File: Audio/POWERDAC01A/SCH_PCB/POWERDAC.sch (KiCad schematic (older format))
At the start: 69 parts, among them J1 CONFIG, J10 BICKI, J11 SA, J12 +VS, J13 -VS, J14 RESET, J15 OUT3, J16 OUT4, J17 OUT1A, J18 OUT1B, J19 OUT2B, J2 DIGITAL POWER, J20 OUT2A, J3 PWRDN, J4 INT_LINE, J5 SDA, J6 SCL, J7 SDI, J8 LRCKI, J9 XTI, M1 HOLE, M2 HOLE, M3 HOLE, M4 HOLE, U1 STA350BW

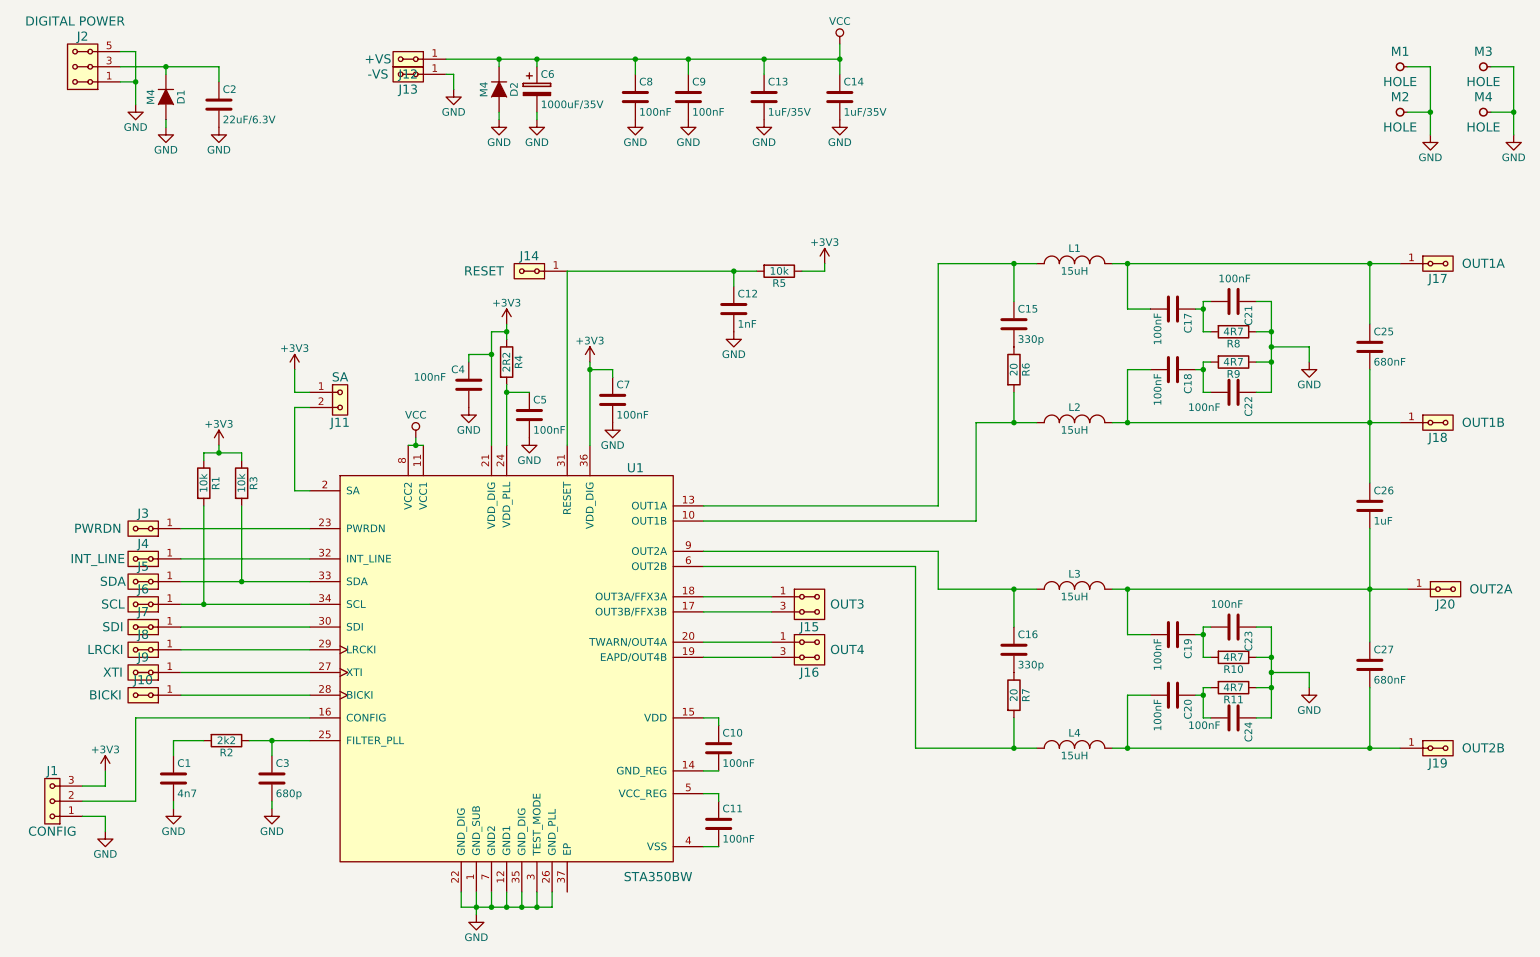
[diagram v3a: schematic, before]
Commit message: routovani plosneho spoje, Zmena zapojeni napajeni konfiguracnich vystupu.
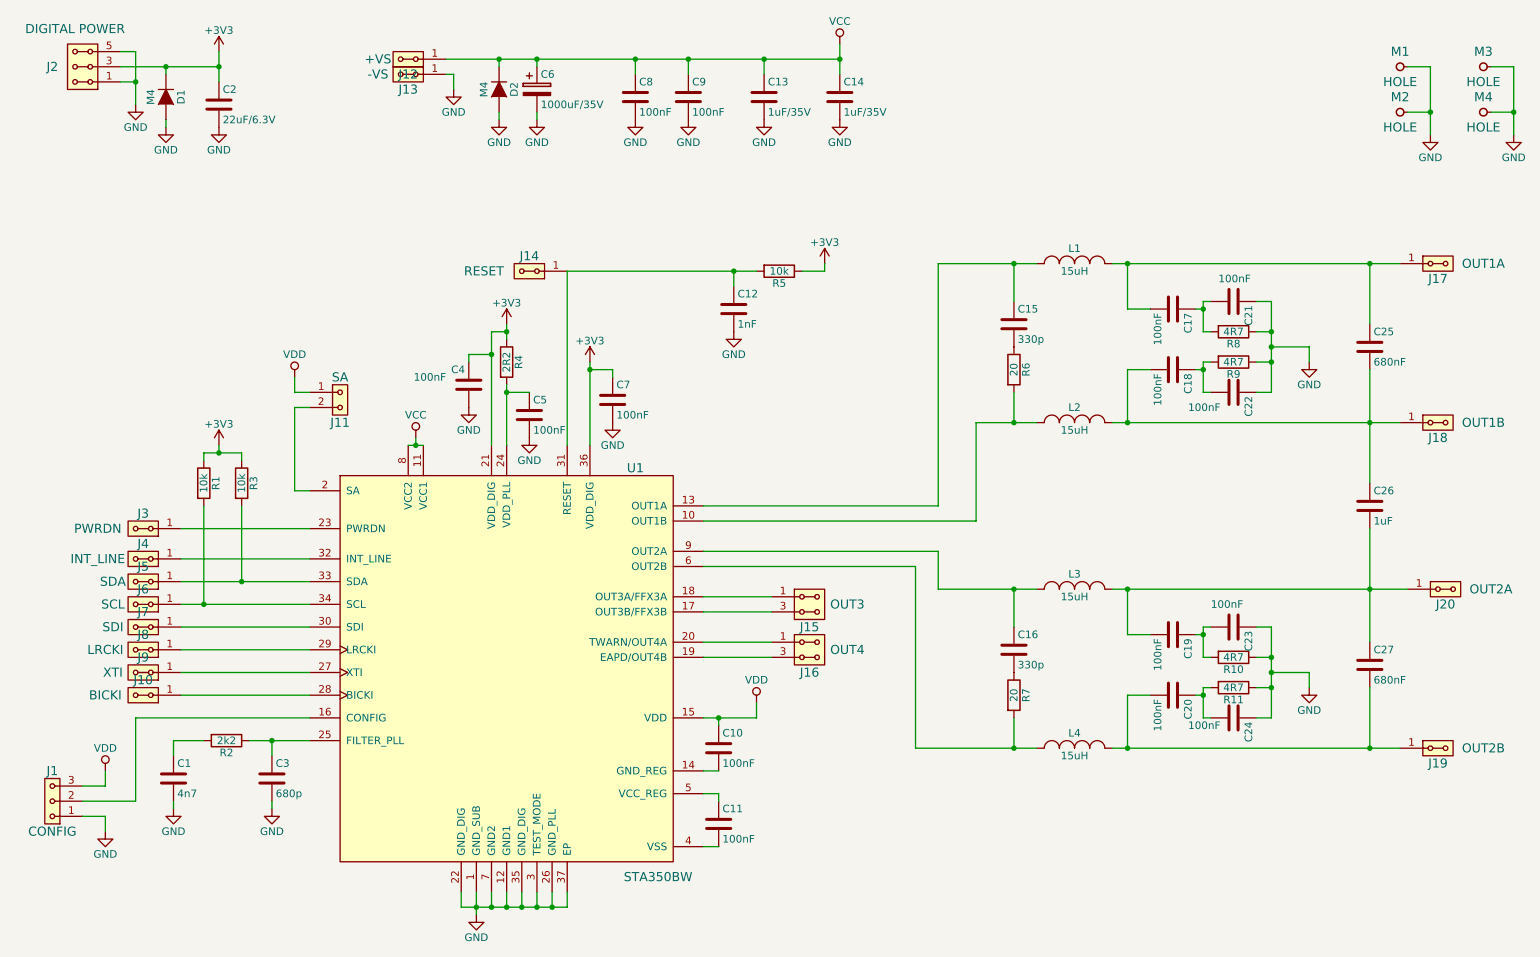
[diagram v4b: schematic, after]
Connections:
- net +3V3: now also C2.1, D1.1 (K), J2.3, J2.4; no longer J1.3, J11.1
- net GND: now also U1.37 (EP)
- net VDD: now reaches C10.1, U1.15 (VDD)
- net VDD: now also J1.3, J11.1
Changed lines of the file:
@@
 	5200 5550 5100 5550
 Wire Wire Line
-	5100 5200 5200 5200
+	5100 5200 5450 5200
 Wire Wire Line
 	5200 5200 5200 5250
@@
 	3500 6350 3500 6450
 Wire Wire Line
-	3500 6450 4100 6450
+	3500 6450 4200 6450
 Wire Wire Line
 	4000 6450 4000 6350
@@
 U 1 1 55FAD3D9
 P 1000 900
-F 0 "J2" H 1000 700 60  0000 C CNN
-F 1 "DIGITAL POWER" H 1050 600 60  0000 C CNN
+F 0 "J2" H 1200 900 60  0000 C CNN
+F 1 "DIGITAL POWER" H 1050 650 60  0000 C CNN
 F 2 "Mlab_Pin_Headers:Straight_2x03" H 1000 1000 60  0001 C CNN
 F 3 "" H 1000 1000 60  0000 C CNN
@@
 $EndComp
 $Comp
-L GND #PWR09
+L GND #PWR08
 U 1 1 55FAD7D5
 P 1350 1150
-F 0 "#PWR09" H 1350 900 50  0001 C CNN
+F 0 "#PWR08" H 1350 900 50  0001 C CNN
 F 1 "GND" H 1350 1000 50  0000 C CNN
 F 2 "" H 1350 1150 60  0000 C CNN
@@
 	1550 900  1550 950
 $Comp
-L GND #PWR010
+L GND #PWR09
 U 1 1 55FAD917
 P 1550 1300
-F 0 "#PWR010" H 1550 1050 50  0001 C CNN
+F 0 "#PWR09" H 1550 1050 50  0001 C CNN
 F 1 "GND" H 1550 1150 50  0000 C CNN
 F 2 "" H 1550 1300 60  0000 C CNN
@@
 $EndComp
 $Comp
-L GND #PWR011
+L GND #PWR010
 U 1 1 55FADC40
 P 5300 2650
-F 0 "#PWR011" H 5300 2400 50  0001 C CNN
+F 0 "#PWR010" H 5300 2400 50  0001 C CNN
 F 1 "GND" H 5300 2500 50  0000 C CNN
 F 2 "" H 5300 2650 60  0000 C CNN
@@
 $EndComp
 $Comp
-L +3V3 #PWR012
+L +3V3 #PWR011
 U 1 1 55FADC46
 P 5900 2200
-F 0 "#PWR012" H 5900 2050 50  0001 C CNN
+F 0 "#PWR011" H 5900 2050 50  0001 C CNN
 F 1 "+3V3" H 5900 2340 50  0000 C CNN
 F 2 "" H 5900 2200 60  0000 C CNN
@@
 $EndComp
 $Comp
-L GND #PWR013
+L GND #PWR012
 U 1 1 55FAE24A
 P 3550 3150
-F 0 "#PWR013" H 3550 2900 50  0001 C CNN
+F 0 "#PWR012" H 3550 2900 50  0001 C CNN
 F 1 "GND" H 3550 3000 50  0000 C CNN
 F 2 "" H 3550 3150 60  0000 C CNN
@@
 Connection ~ 3800 2650
 $Comp
-L GND #PWR014
+L GND #PWR013
 U 1 1 55FAE676
 P 1900 1300
-F 0 "#PWR014" H 1900 1050 50  0001 C CNN
+F 0 "#PWR013" H 1900 1050 50  0001 C CNN
 F 1 "GND" H 1900 1150 50  0000 C CNN
 F 2 "" H 1900 1300 60  0000 C CNN
@@
 $EndComp
 Wire Wire Line
-	1900 900  1900 1000
+	1900 800  1900 1000
 Connection ~ 1550 900
 $Comp
@@
 $EndComp
 $Comp
-L GND #PWR015
+L GND #PWR014
 U 1 1 55FAD2D2
 P 4000 1250
-F 0 "#PWR015" H 4000 1000 50  0001 C CNN
+F 0 "#PWR014" H 4000 1000 50  0001 C CNN
 F 1 "GND" H 4000 1100 50  0000 C CNN
 F 2 "" H 4000 1250 60  0000 C CNN
@@
 	4000 850  4000 900
 $Comp
-L GND #PWR016
+L GND #PWR015
 U 1 1 55FAD76F
 P 3450 1050
-F 0 "#PWR016" H 3450 800 50  0001 C CNN
+F 0 "#PWR015" H 3450 800 50  0001 C CNN
 F 1 "GND" H 3450 900 50  0000 C CNN
 F 2 "" H 3450 1050 60  0000 C CNN
@@
 	3750 850  3750 900
 $Comp
-L GND #PWR017
+L GND #PWR016
 U 1 1 55FADBDD
 P 3750 1250
-F 0 "#PWR017" H 3750 1000 50  0001 C CNN
+F 0 "#PWR016" H 3750 1000 50  0001 C CNN
 F 1 "GND" H 3750 1100 50  0000 C CNN
 F 2 "" H 3750 1250 60  0000 C CNN
@@
 $EndComp
 $Comp
-L GND #PWR018
+L GND #PWR017
 U 1 1 55FAE3B8
 P 2250 5800
-F 0 "#PWR018" H 2250 5550 50  0001 C CNN
+F 0 "#PWR017" H 2250 5550 50  0001 C CNN
 F 1 "GND" H 2250 5650 50  0000 C CNN
 F 2 "" H 2250 5800 60  0000 C CNN
@@
 $EndComp
 $Comp
-L GND #PWR019
+L GND #PWR018
 U 1 1 55FAE3E0
 P 1600 5800
-F 0 "#PWR019" H 1600 5550 50  0001 C CNN
+F 0 "#PWR018" H 1600 5550 50  0001 C CNN
 F 1 "GND" H 1600 5650 50  0000 C CNN
 F 2 "" H 1600 5800 60  0000 C CNN
@@
 $EndComp
 $Comp
-L GND #PWR020
+L GND #PWR019
 U 1 1 55FAFAB6
 P 4650 1250
-F 0 "#PWR020" H 4650 1000 50  0001 C CNN
+F 0 "#PWR019" H 4650 1000 50  0001 C CNN
 F 1 "GND" H 4650 1100 50  0000 C CNN
 F 2 "" H 4650 1250 60  0000 C CNN
@@
 $EndComp
 $Comp
-L GND #PWR021
+L GND #PWR020
 U 1 1 55FAFC49
 P 5000 1250
-F 0 "#PWR021" H 5000 1000 50  0001 C CNN
+F 0 "#PWR020" H 5000 1000 50  0001 C CNN
 F 1 "GND" H 5000 1100 50  0000 C CNN
 F 2 "" H 5000 1250 60  0000 C CNN
@@
 $EndComp
 $Comp
-L GND #PWR022
+L GND #PWR021
 U 1 1 55FAFC9F
 P 5500 1250
-F 0 "#PWR022" H 5500 1000 50  0001 C CNN
+F 0 "#PWR021" H 5500 1000 50  0001 C CNN
 F 1 "GND" H 5500 1100 50  0000 C CNN
 F 2 "" H 5500 1250 60  0000 C CNN
@@
 $EndComp
 $Comp
-L GND #PWR023
+L GND #PWR022
 U 1 1 55FB00F6
 P 6000 1250
-F 0 "#PWR023" H 6000 1000 50  0001 C CNN
+F 0 "#PWR022" H 6000 1000 50  0001 C CNN
 F 1 "GND" H 6000 1100 50  0000 C CNN
 F 2 "" H 6000 1250 60  0000 C CNN
@@
 Connection ~ 6000 850
 $Comp
-L VCC #PWR025
+L VCC #PWR023
 U 1 1 55FBE7BF
 P 6000 750
-F 0 "#PWR025" H 6000 600 50  0001 C CNN
+F 0 "#PWR023" H 6000 600 50  0001 C CNN
 F 1 "VCC" H 6000 900 50  0000 C CNN
 F 2 "" H 6000 750 60  0000 C CNN
@@
 $EndComp
 $Comp
-L VCC #PWR026
+L VCC #PWR024
 U 1 1 55FBEA63
 P 3200 3350
-F 0 "#PWR026" H 3200 3200 50  0001 C CNN
+F 0 "#PWR024" H 3200 3200 50  0001 C CNN
 F 1 "VCC" H 3200 3500 50  0000 C CNN
 F 2 "" H 3200 3350 60  0000 C CNN
@@
 	1    0    0    -1
 $EndComp
-$Comp
-L +3V3 #PWR027
-U 1 1 55FBFD8F
-P 2400 2900
-F 0 "#PWR027" H 2400 2750 50  0001 C CNN
-F 1 "+3V3" H 2400 3040 50  0000 C CNN
-F 2 "" H 2400 2900 60  0000 C CNN
-F 3 "" H 2400 2900 60  0000 C CNN
-	1    2400 2900
-	1    0    0    -1
-$EndComp
-Wire Wire Line
-	2400 2900 2400 3050
 Wire Wire Line
 	2400 3050 2500 3050
@@
 $EndComp
 $Comp
-L GND #PWR028
+L GND #PWR025
 U 1 1 55FC253F
 P 9100 2850
-F 0 "#PWR028" H 9100 2600 50  0001 C CNN
+F 0 "#PWR025" H 9100 2600 50  0001 C CNN
 F 1 "GND" H 9100 2700 50  0000 C CNN
 F 2 "" H 9100 2850 60  0000 C CNN
@@
 $EndComp
 $Comp
-L GND #PWR029
+L GND #PWR026
 U 1 1 55FC600B
 P 9100 5000
-F 0 "#PWR029" H 9100 4750 50  0001 C CNN
+F 0 "#PWR026" H 9100 4750 50  0001 C CNN
 F 1 "GND" H 9100 4850 50  0000 C CNN
 F 2 "" H 9100 5000 60  0000 C CNN
@@
 $EndComp
 $Comp
-L GND #PWR030
+L GND #PWR027
 U 1 1 55FCC040
 P 1150 5950
-F 0 "#PWR030" H 1150 5700 50  0001 C CNN
+F 0 "#PWR027" H 1150 5700 50  0001 C CNN
 F 1 "GND" H 1150 5800 50  0000 C CNN
 F 2 "" H 1150 5950 60  0000 C CNN
 F 3 "" H 1150 5950 60  0000 C CNN
 	1    1150 5950
-	1    0    0    -1
-$EndComp
-$Comp
-L +3V3 #PWR031
-U 1 1 55FCC08A
-P 1150 5550
-F 0 "#PWR031" H 1150 5400 50  0001 C CNN
-F 1 "+3V3" H 1150 5690 50  0000 C CNN
-F 2 "" H 1150 5550 60  0000 C CNN
-F 3 "" H 1150 5550 60  0000 C CNN
-	1    1150 5550
 	1    0    0    -1
 $EndComp
@@
 Connection ~ 4000 6450
 $Comp
-L GND #PWR?
+L GND #PWR028
 U 1 1 56007D42
 P 3950 3350
-F 0 "#PWR?" H 3950 3100 50  0001 C CNN
+F 0 "#PWR028" H 3950 3100 50  0001 C CNN
 F 1 "GND" H 3950 3200 50  0000 C CNN
 F 2 "" H 3950 3350 60  0000 C CNN
@@
 	1    0    0    -1
 $EndComp
+Wire Wire Line
+	4200 6450 4200 6350
+Connection ~ 4100 6450
+$Comp
+L VDD #PWR029
+U 1 1 5602BA33
+P 5450 5100
+F 0 "#PWR029" H 5450 4950 50  0001 C CNN
+F 1 "VDD" H 5450 5250 50  0000 C CNN
+F 2 "" H 5450 5100 60  0000 C CNN
+F 3 "" H 5450 5100 60  0000 C CNN
+	1    5450 5100
+	1    0    0    -1
+$EndComp
+Wire Wire Line
+	5450 5200 5450 5100
+Connection ~ 5200 5200
+$Comp
+L VDD #PWR030
+U 1 1 5602C076
+P 2400 2950
+F 0 "#PWR030" H 2400 2800 50  0001 C CNN
+F 1 "VDD" H 2400 3100 50  0000 C CNN
+F 2 "" H 2400 2950 60  0000 C CNN
+F 3 "" H 2400 2950 60  0000 C CNN
+	1    2400 2950
+	1    0    0    -1
+$EndComp
+Wire Wire Line
+	2400 3050 2400 2950
+$Comp
+L VDD #PWR031
+U 1 1 5602CAC9
+P 1150 5550
+F 0 "#PWR031" H 1150 5400 50  0001 C CNN
+F 1 "VDD" H 1150 5700 50  0000 C CNN
+F 2 "" H 1150 5550 60  0000 C CNN
+F 3 "" H 1150 5550 60  0000 C CNN
+	1    1150 5550
+	1    0    0    -1
+$EndComp
+$Comp
+L +3V3 #PWR?
+U 1 1 5602D1C3
+P 1900 800
+F 0 "#PWR?" H 1900 650 50  0001 C CNN
+F 1 "+3V3" H 1900 940 50  0000 C CNN
+F 2 "" H 1900 800 60  0000 C CNN
+F 3 "" H 1900 800 60  0000 C CNN
+	1    1900 800
+	1    0    0    -1
+$EndComp
+Connection ~ 1900 900
 $EndSCHEMATC

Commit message: posunutin popisku v silkscreen.
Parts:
- D2: footprint Diodes_SMD:SMA_Standard -> Diodes_SMD:SMB_Handsoldering
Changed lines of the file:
@@
 F 0 "D2" H 3750 1150 50  0000 C CNN
 F 1 "M4" H 3750 950 50  0000 C CNN
-F 2 "Diodes_SMD:SMA_Standard" H 3750 1050 60  0001 C CNN
+F 2 "Diodes_SMD:SMB_Handsoldering" H 3750 1050 60  0001 C CNN
 F 3 "" H 3750 1050 60  0000 C CNN
 	1    3750 1050
